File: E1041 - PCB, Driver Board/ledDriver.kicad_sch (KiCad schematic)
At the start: 31 parts, among them J10 Conn_01x05_Pin, J11 Conn_01x05_Pin, J12 Conn_01x05_Pin, J13 Conn_01x05_Pin, J14 Conn_01x05_Pin, J15 Conn_01x05_Pin, J16 Conn_01x05_Pin, J17 Conn_01x05_Pin, J18 Conn_01x05_Pin, J19 Conn_01x05_Pin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

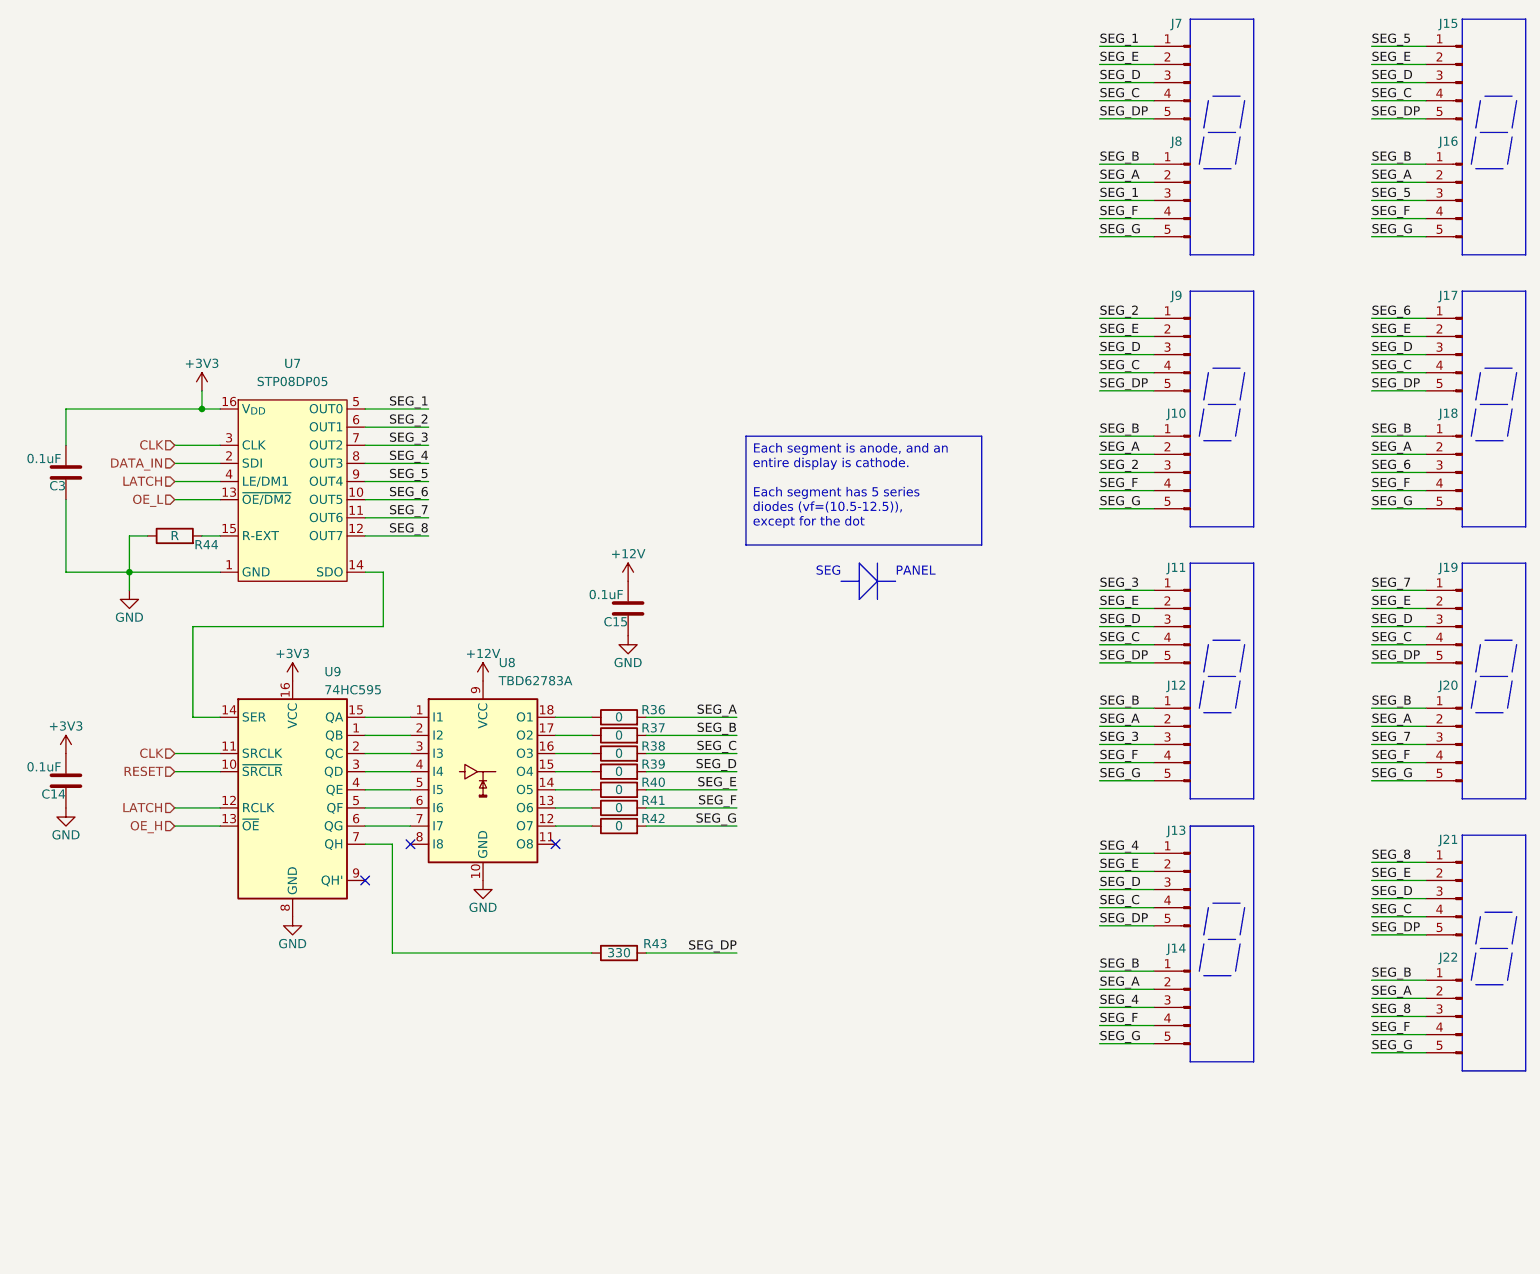
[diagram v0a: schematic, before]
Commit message: Added 'Part Number' in schematic, no design change
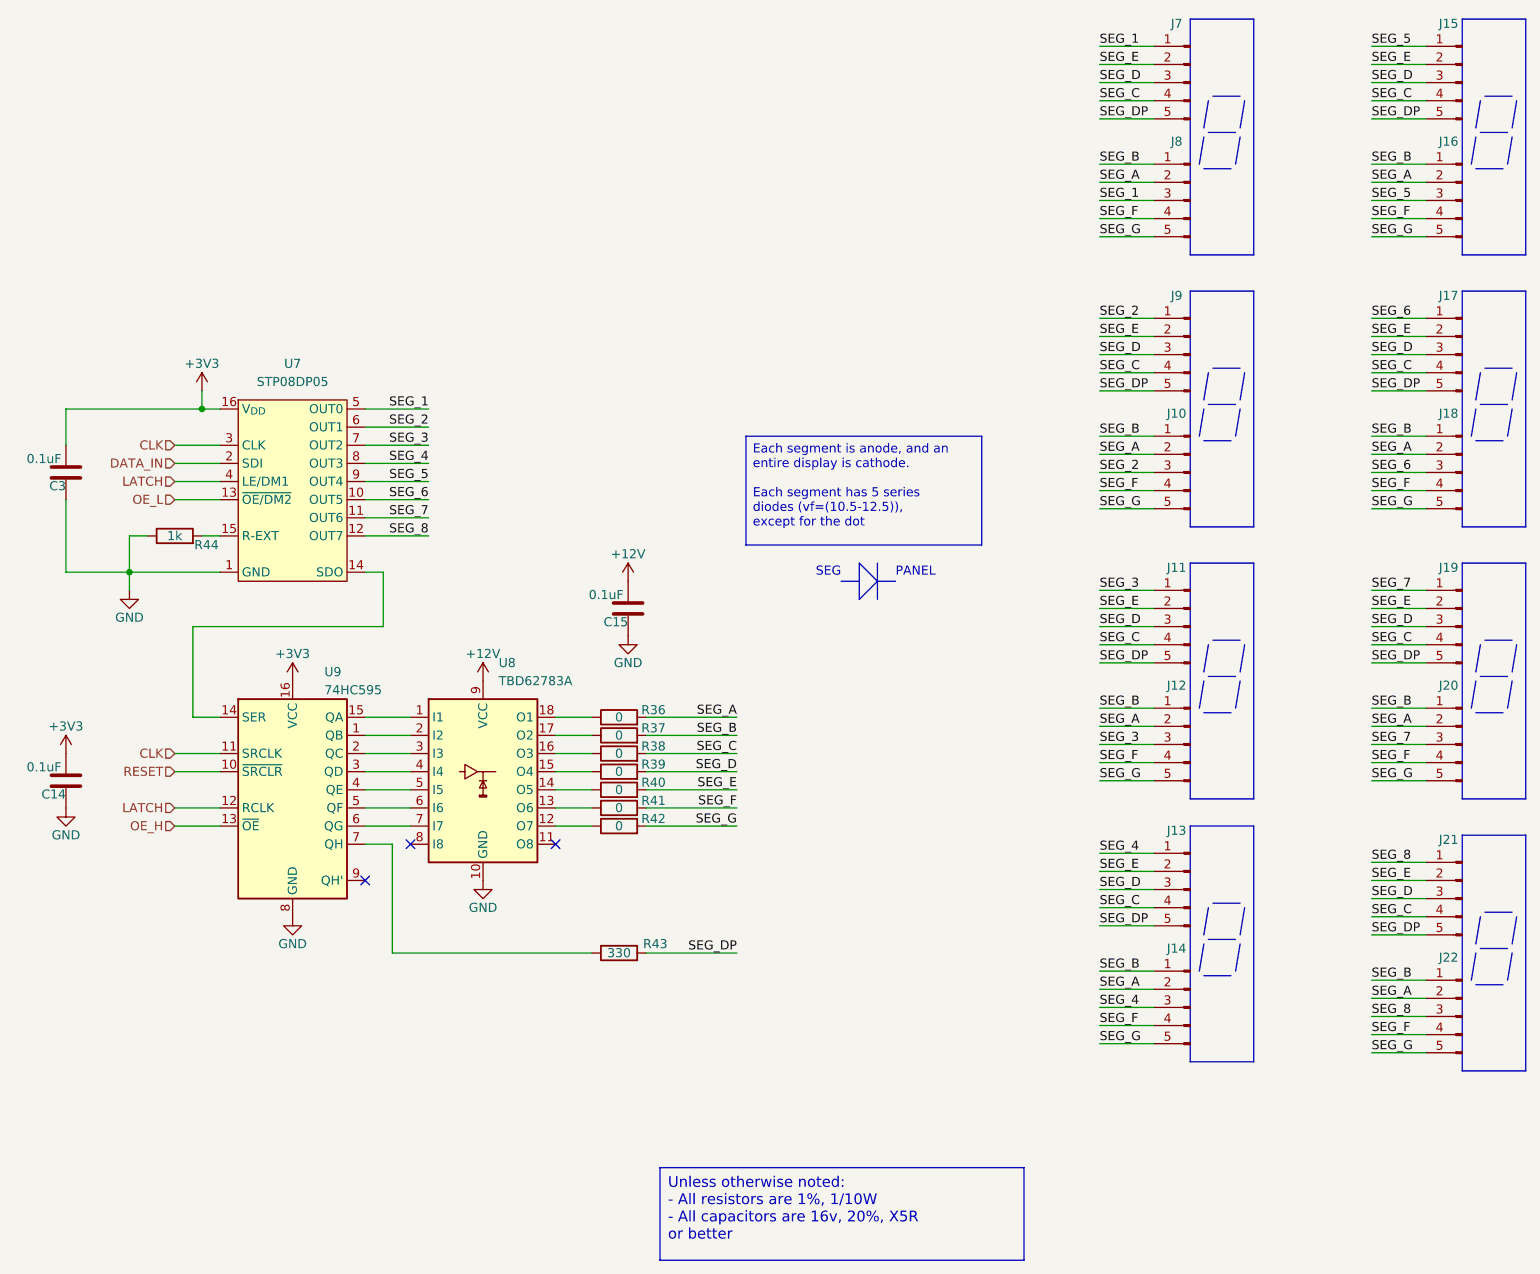
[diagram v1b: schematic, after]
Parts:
- J10, J11, J12, J13, J14, J15, J16, J17, J18, J19, J20, J21, J22, J7, J8, J9: Part Number (none) -> B5B-PH-K-S
- R44: value R -> 1k
- U7: Part Number (none) -> STP08DP05
- U8: Part Number (none) -> TBD62783A
- U9: Part Number (none) -> 74HC595
